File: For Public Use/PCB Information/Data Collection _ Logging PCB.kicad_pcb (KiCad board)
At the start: 2 copper layers, 35.6 x 53.3 mm, 8 parts, among them U1 TC2014-3.3VxCTTR

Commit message: Redid the current PCB Information
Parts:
- Micro_SD1, RT1: footprint Connector_PinSocket_1.00mm:PinSocket_1x06_P1.00mm_Vertical -> Connector_PinSocket_2.54mm:PinSocket_1x06_P2.54mm_Vertical
- US1, US2: footprint Connector_PinSocket_1.00mm:PinSocket_1x04_P1.00mm_Vertical -> Connector_PinSocket_2.54mm:PinSocket_1x04_P2.54mm_Vertical
- moved US2 51.9 mm to (194.3, 81.9)
- moved C1 48.2 mm to (193.0, 99.1)
- moved US1 48.1 mm to (187.3, 81.9)
- moved U1 46.1 mm to (187.3, 99.1)
- moved Micro_SD1 42.3 mm to (188.0, 108.0)
- moved C2 39.2 mm to (181.0, 99.1)
- moved XA1 37.4 mm to (104.1, 127.0)
- moved RT1 16.5 mm to (177.8, 108.0)
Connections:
- C2 pad 2: Net-(RT1-VCC) -> Net-(U1-VIN)
- RT1 pad 5: Net-(RT1-VCC) -> Net-(Micro_SD1-3.3V)
- U1 pad 1: Net-(RT1-VCC) -> Net-(U1-VIN)
- US1 pad 4: Net-(RT1-VCC) -> Net-(U1-VIN)
- US2 pad 4: Net-(RT1-VCC) -> Net-(U1-VIN)
- XA1 pad 5V3: Net-(RT1-VCC) -> Net-(U1-VIN)
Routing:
- net Net-(RT1-VCC): track 61.7 -> 0.00 mm
- net Net-(U1-VIN): track 0.00 -> 36.5 mm
- net Net-(RT1-SCL): track 14.0 -> 47.2 mm
- net Net-(RT1-~{INT}/SQW): track 8.65 -> 36.4 mm
- net Net-(RT1-SDA): track 19.1 -> 44.0 mm
- net Net-(Micro_SD1-3.3V): track 19.4 -> 39.3 mm
- net Net-(US2-ECHO): track 13.7 -> 31.5 mm
- net Net-(US1-ECHO): track 14.5 -> 29.2 mm
- net Net-(US1-TRIG): track 18.0 -> 32.2 mm
- net Net-(Micro_SD1-CS): track 15.0 -> 20.3 mm
- net Net-(Micro_SD1-MOSI): track 15.0 -> 13.2 mm
- net Net-(US2-TRIG): track 21.7 -> 23.3 mm
- net Net-(Micro_SD1-CLK): track 11.7 -> 10.7 mm
- net Net-(Micro_SD1-MISO): track 12.3 -> 11.7 mm
- net GND: vias 9 -> 10
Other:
- board size 35.6 x 53.3 mm -> 34.3 x 53.3 mm
- board text added: "Datalogging v0.2 5/16/2024 Nicholas Liger ARTS Lab - USC"
- board text removed: "Datalogging Board v1.0 5/10/2024 Nicholas Liger ARTS Lab - USC"

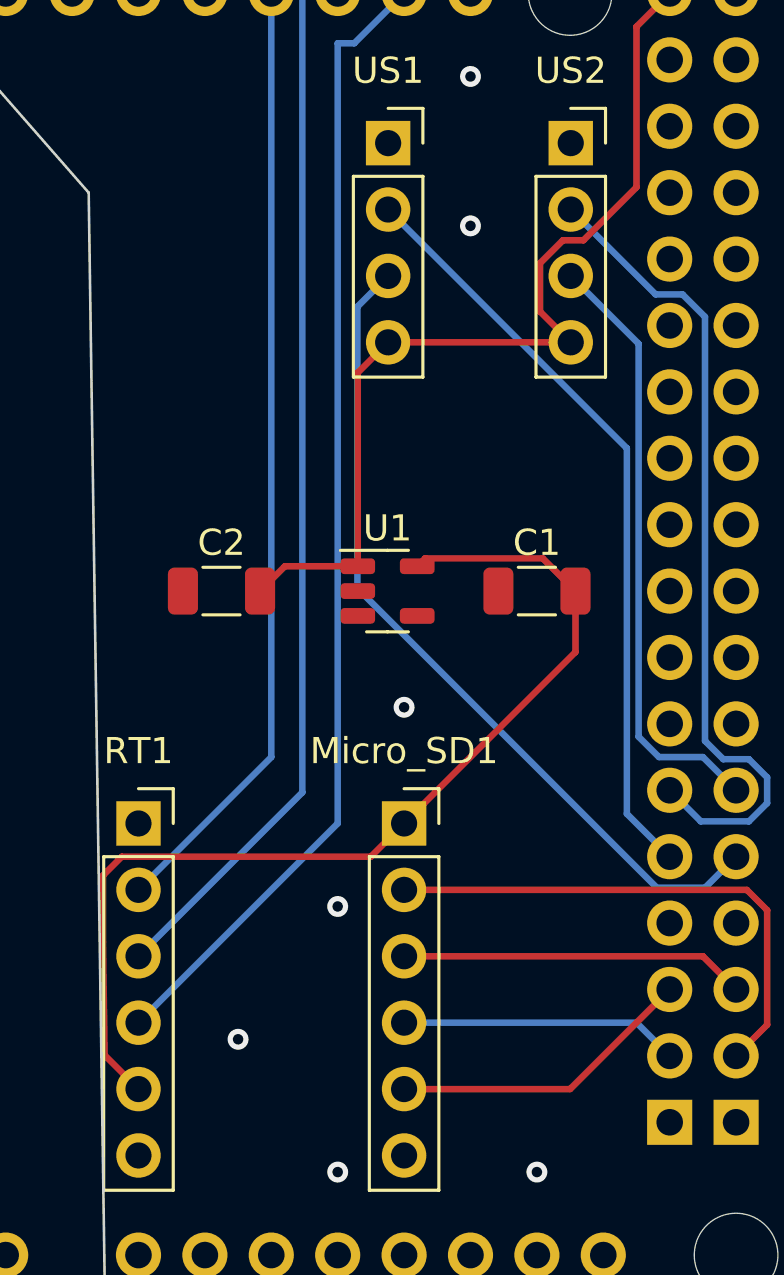
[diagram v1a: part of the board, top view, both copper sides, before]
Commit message: Added labels to datalogging board
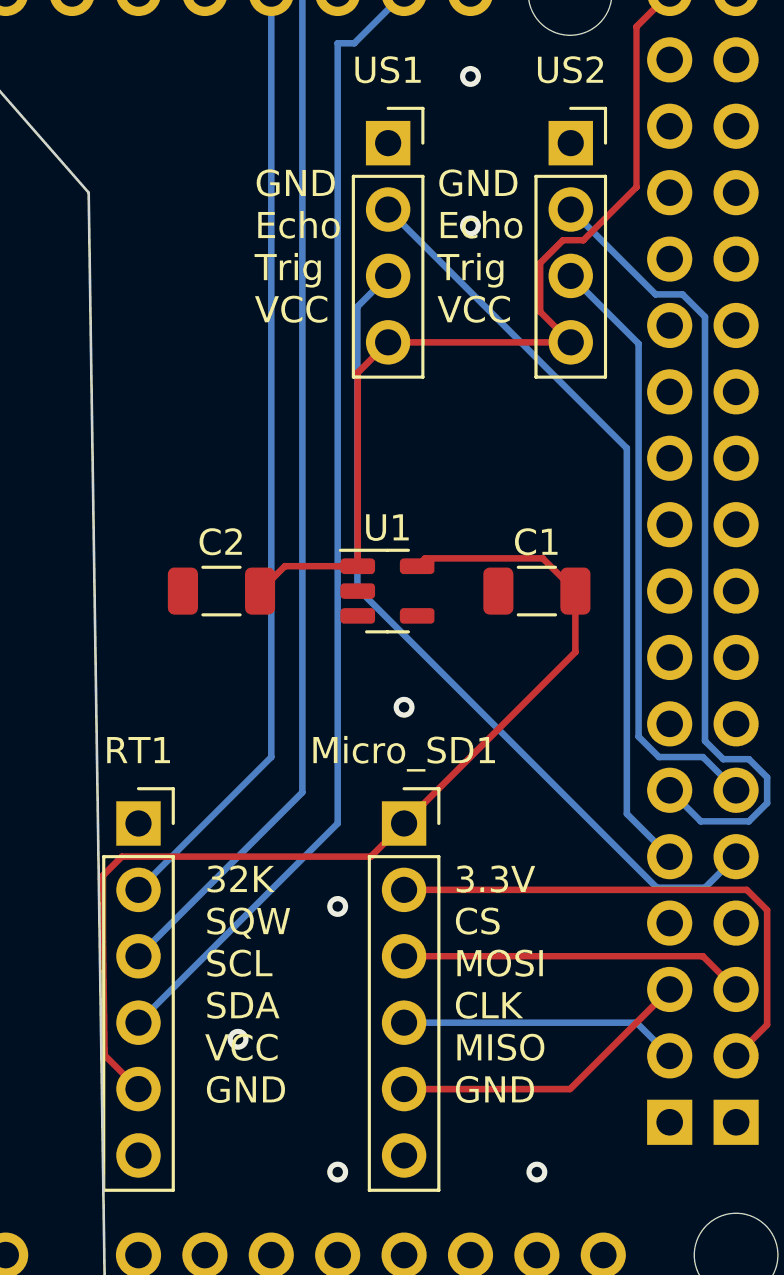
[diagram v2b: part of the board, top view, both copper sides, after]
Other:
- board text added: "3.3V CS MOSI CLK MISO GND"
- board text added: "32K SQW SCL SDA VCC GND"
- board text added: "GND Echo Trig VCC"
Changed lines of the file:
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@@
     (effects (font (size 1 1) (thickness 0.15)) (justify left bottom mirror))
+  )
+  (gr_text "GND\nEcho\nTrig\nVCC" (at 189.23 88.9) (layer "F.SilkS")
+    (effects (font (size 1 1) (thickness 0.15)) (justify left bottom))
+  )
+  (gr_text "32K\nSQW\nSCL\nSDA\nVCC\nGND" (at 180.34 118.745) (layer "F.SilkS")
+    (effects (font (size 1 1) (thickness 0.15)) (justify left bottom))
+  )
+  (gr_text "GND\nEcho\nTrig\nVCC" (at 182.245 88.9) (layer "F.SilkS")
+    (effects (font (size 1 1) (thickness 0.15)) (justify left bottom))
+  )
+  (gr_text "3.3V\nCS\nMOSI\nCLK\nMISO\nGND" (at 189.865 118.745) (layer "F.SilkS")
+    (effects (font (size 1 1) (thickness 0.15)) (justify left bottom))
   )
   (via (at 203.835 120.65) (size 0.8) (drill 0.4) (layers "F.Cu" "B.Cu") (free) (net 1))
